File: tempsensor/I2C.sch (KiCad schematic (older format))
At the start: 19 parts, among them J2 Conn_01x04, U2 24C16, U3 MCP9844, U4 SN74LVC2T45DCUR, U5 SN74LVC2T45DCUR

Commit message: Added footprints to tempsensor.
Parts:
- J2: footprint Connector_PinHeader_2.54mm:PinHeader_1x04_P2.54mm_Vertical -> Connector_PinHeader_2.54mm:PinHeader_2x02_P2.54mm_Vertical
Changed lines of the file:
@@
 F 0 "J2" H 3880 7242 50  0000 L CNN
 F 1 "Conn_01x04" H 3880 7151 50  0000 L CNN
-F 2 "Connector_PinHeader_2.54mm:PinHeader_1x04_P2.54mm_Vertical" H 3800 7250 50  0001 C CNN
+F 2 "Connector_PinHeader_2.54mm:PinHeader_2x02_P2.54mm_Vertical" H 3800 7250 50  0001 C CNN
 F 3 "~" H 3800 7250 50  0001 C CNN
 	1    3800 7250

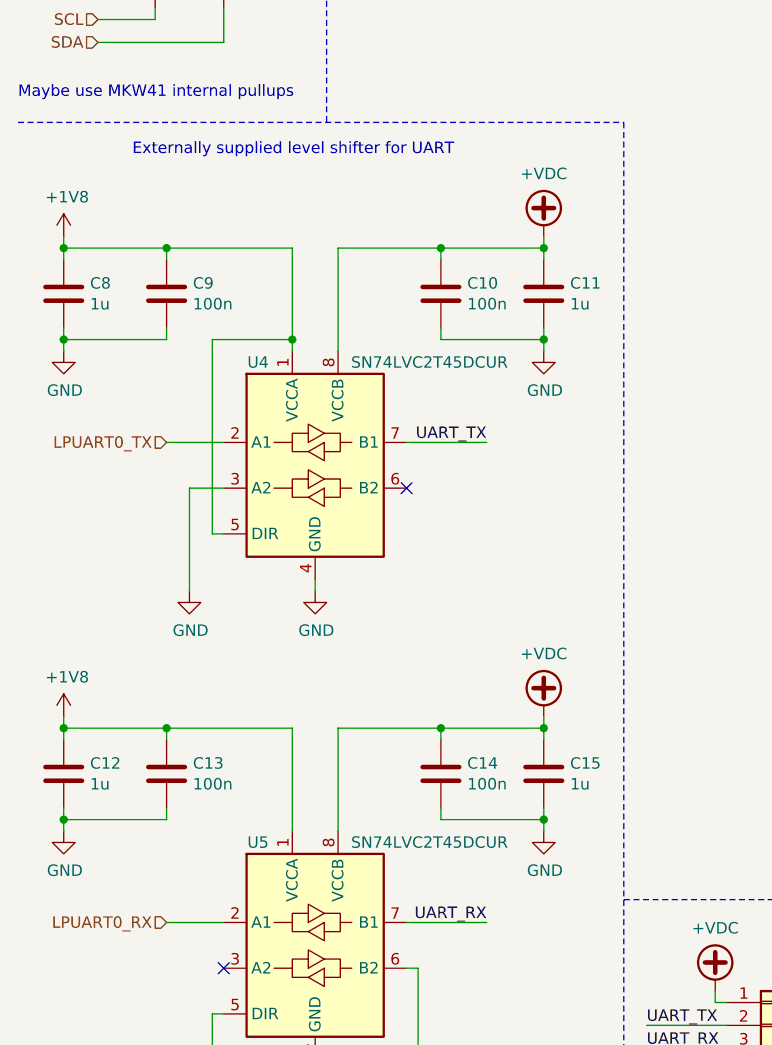
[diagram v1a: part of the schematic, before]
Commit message: Started layouting the TempSensor, exchanged the large LEDs for 0603 LEDs (from ELAB). MCU needs to be placed. Changed signals on expansion header to put power pins onto just one end.
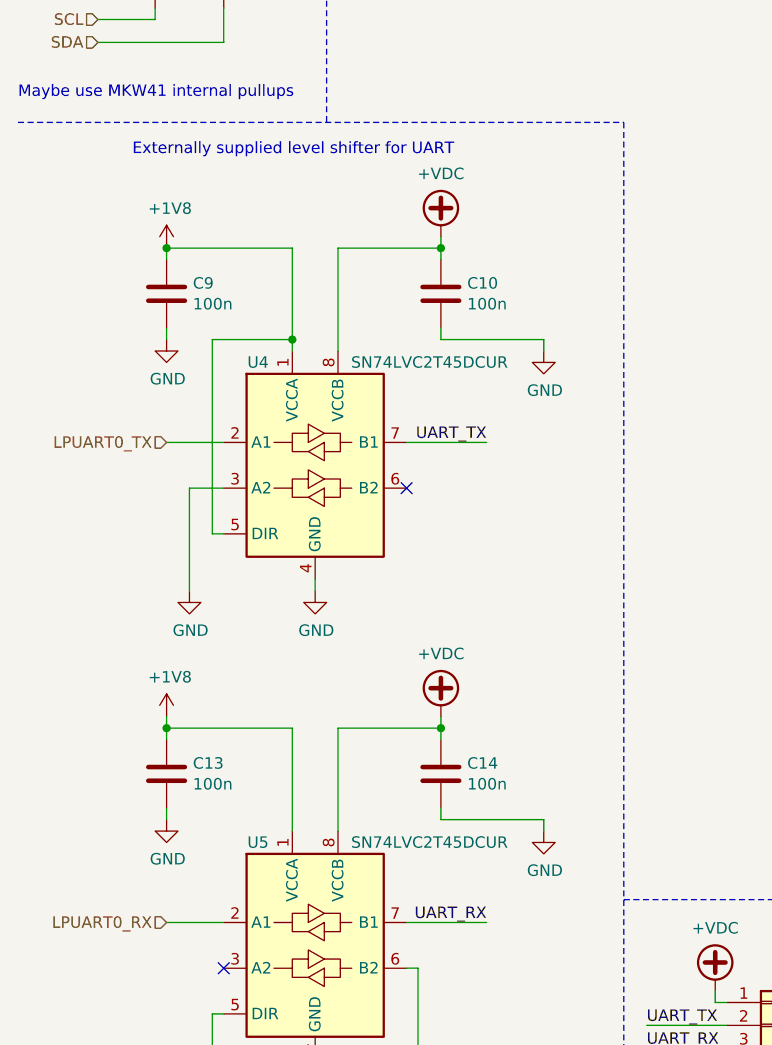
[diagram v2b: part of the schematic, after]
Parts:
- removed C11, C12, C15, C8: 1u, Capacitor_SMD:C_0402_1005Metric, symbol Device:C
- R4: footprint Resistor_SMD:R_0603_1608Metric -> Resistor_SMD:R_0402_1005Metric
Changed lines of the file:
@@
 F 0 "R4" V 5743 3800 50  0000 C CNN
 F 1 "R" V 5834 3800 50  0000 C CNN
-F 2 "Resistor_SMD:R_0603_1608Metric" V 5880 3800 50  0001 C CNN
+F 2 "Resistor_SMD:R_0402_1005Metric" V 5880 3800 50  0001 C CNN
 F 3 "~" H 5950 3800 50  0001 C CNN
 	1    5950 3800
@@
 $Comp
 L Device:C C?
-U 1 1 5FAF3E79
-P 700 4050
-AR Path="/5FAF3E79" Ref="C?"  Part="1"
-AR Path="/5FA4227D/5FAF3E79" Ref="C8"  Part="1"
-F 0 "C8" H 815 4096 50  0000 L CNN
-F 1 "1u" H 815 4005 50  0000 L CNN
-F 2 "Capacitor_SMD:C_0402_1005Metric" H 738 3900 50  0001 C CNN
-F 3 "~" H 700 4050 50  0001 C CNN
-	1    700  4050
-	1    0    0    -1
-$EndComp
-$Comp
-L Device:C C?
 U 1 1 5FAF3E7F
 P 2350 4050
@@
 $EndComp
 $Comp
-L Device:C C?
-U 1 1 5FAF3E85
-P 2800 4050
-AR Path="/5FAF3E85" Ref="C?"  Part="1"
-AR Path="/5FA4227D/5FAF3E85" Ref="C11"  Part="1"
-F 0 "C11" H 2915 4096 50  0000 L CNN
-F 1 "1u" H 2915 4005 50  0000 L CNN
-F 2 "Capacitor_SMD:C_0402_1005Metric" H 2838 3900 50  0001 C CNN
-F 3 "~" H 2800 4050 50  0001 C CNN
-	1    2800 4050
-	1    0    0    -1
-$EndComp
-$Comp
 L power:GND #PWR?
 U 1 1 5FAF3E8B
@@
 	2350 4250 2800 4250
 Wire Wire Line
-	2800 4200 2800 4250
-Wire Wire Line
 	1900 4300 1900 3850
 Wire Wire Line
 	1900 3850 2350 3850
-Wire Wire Line
-	2800 3850 2800 3900
 Wire Wire Line
 	2350 3850 2350 3900
 Connection ~ 2350 3850
 Wire Wire Line
-	2350 3850 2800 3850
-Wire Wire Line
 	1700 4300 1700 4250
 Wire Wire Line
 	1700 3850 1150 3850
 Wire Wire Line
-	700  3850 700  3900
-Wire Wire Line
 	1150 3900 1150 3850
-Connection ~ 1150 3850
-Wire Wire Line
-	1150 3850 700  3850
 Wire Wire Line
 	2800 4300 2800 4250
-Connection ~ 2800 4250
 $Comp
 L power:GND #PWR?
 U 1 1 5FAF3EA2
-P 700 4300
+P 1150 4250
 AR Path="/5FAF3EA2" Ref="#PWR?"  Part="1"
 AR Path="/5FA4227D/5FAF3EA2" Ref="#PWR027"  Part="1"
-F 0 "#PWR027" H 700 4050 50  0001 C CNN
-F 1 "GND" H 705 4127 50  0000 C CNN
-F 2 "" H 700 4300 50  0001 C CNN
-F 3 "" H 700 4300 50  0001 C CNN
-	1    700  4300
-	1    0    0    -1
-$EndComp
-Wire Wire Line
-	700  4200 700  4250
+F 0 "#PWR027" H 1150 4000 50  0001 C CNN
+F 1 "GND" H 1155 4077 50  0000 C CNN
+F 2 "" H 1150 4250 50  0001 C CNN
+F 3 "" H 1150 4250 50  0001 C CNN
+	1    1150 4250
+	1    0    0    -1
+$EndComp
 Wire Wire Line
 	1150 4200 1150 4250
-Wire Wire Line
-	1150 4250 700  4250
-Connection ~ 700  4250
-Wire Wire Line
-	700  4250 700  4300
 $Comp
 L power:+1V8 #PWR?
 U 1 1 5FAF3EAD
-P 700 3800
+P 1150 3850
 AR Path="/5FAF3EAD" Ref="#PWR?"  Part="1"
 AR Path="/5FA4227D/5FAF3EAD" Ref="#PWR025"  Part="1"
-F 0 "#PWR025" H 700 3650 50  0001 C CNN
-F 1 "+1V8" H 715 3973 50  0000 C CNN
-F 2 "" H 700 3800 50  0001 C CNN
-F 3 "" H 700 3800 50  0001 C CNN
-	1    700  3800
-	1    0    0    -1
-$EndComp
-Wire Wire Line
-	700  3800 700  3850
-Connection ~ 700  3850
+F 0 "#PWR025" H 1150 3700 50  0001 C CNN
+F 1 "+1V8" H 1165 4023 50  0000 C CNN
+F 2 "" H 1150 3850 50  0001 C CNN
+F 3 "" H 1150 3850 50  0001 C CNN
+	1    1150 3850
+	1    0    0    -1
+$EndComp
 Text Label 2550 4700 2    50   ~ 0
 UART_TX
@@
 Wire Wire Line
 	1150 4700 1400 4700
-Wire Wire Line
-	2800 3800 2800 3850
-Connection ~ 2800 3850
 $Comp
 L Logic_LevelTranslator:SN74LVC2T45DCUR U?
@@
 $Comp
 L Device:C C?
-U 1 1 5FAF3EDB
-P 700 6150
-AR Path="/5FAF3EDB" Ref="C?"  Part="1"
-AR Path="/5FA4227D/5FAF3EDB" Ref="C12"  Part="1"
-F 0 "C12" H 815 6196 50  0000 L CNN
-F 1 "1u" H 815 6105 50  0000 L CNN
-F 2 "Capacitor_SMD:C_0402_1005Metric" H 738 6000 50  0001 C CNN
-F 3 "~" H 700 6150 50  0001 C CNN
-	1    700  6150
-	1    0    0    -1
-$EndComp
-$Comp
-L Device:C C?
 U 1 1 5FAF3EE1
 P 2350 6150
@@
 $EndComp
 $Comp
-L Device:C C?
-U 1 1 5FAF3EE7
-P 2800 6150
-AR Path="/5FAF3EE7" Ref="C?"  Part="1"
-AR Path="/5FA4227D/5FAF3EE7" Ref="C15"  Part="1"
-F 0 "C15" H 2915 6196 50  0000 L CNN
-F 1 "1u" H 2915 6105 50  0000 L CNN
-F 2 "Capacitor_SMD:C_0402_1005Metric" H 2838 6000 50  0001 C CNN
-F 3 "~" H 2800 6150 50  0001 C CNN
-	1    2800 6150
-	1    0    0    -1
-$EndComp
-$Comp
 L power:GND #PWR?
 U 1 1 5FAF3EED
@@
 	2350 6350 2800 6350
 Wire Wire Line
-	2800 6300 2800 6350
-Wire Wire Line
 	1900 6400 1900 5950
 Wire Wire Line
 	1900 5950 2350 5950
-Wire Wire Line
-	2800 5950 2800 6000
 Wire Wire Line
 	2350 5950 2350 6000
 Connection ~ 2350 5950
 Wire Wire Line
-	2350 5950 2800 5950
-Wire Wire Line
 	1700 5950 1150 5950
 Wire Wire Line
-	700  5950 700  6000
-Wire Wire Line
 	1150 6000 1150 5950
-Connection ~ 1150 5950
-Wire Wire Line
-	1150 5950 700  5950
 Wire Wire Line
 	2800 6400 2800 6350
-Connection ~ 2800 6350
 $Comp
 L power:GND #PWR?
 U 1 1 5FAF3F03
-P 700 6400
+P 1150 6350
 AR Path="/5FAF3F03" Ref="#PWR?"  Part="1"
 AR Path="/5FA4227D/5FAF3F03" Ref="#PWR035"  Part="1"
-F 0 "#PWR035" H 700 6150 50  0001 C CNN
-F 1 "GND" H 705 6227 50  0000 C CNN
-F 2 "" H 700 6400 50  0001 C CNN
-F 3 "" H 700 6400 50  0001 C CNN
-	1    700  6400
-	1    0    0    -1
-$EndComp
-Wire Wire Line
-	700  6300 700  6350
+F 0 "#PWR035" H 1150 6100 50  0001 C CNN
+F 1 "GND" H 1155 6177 50  0000 C CNN
+F 2 "" H 1150 6350 50  0001 C CNN
+F 3 "" H 1150 6350 50  0001 C CNN
+	1    1150 6350
+	1    0    0    -1
+$EndComp
 Wire Wire Line
 	1150 6300 1150 6350
-Wire Wire Line
-	1150 6350 700  6350
-Connection ~ 700  6350
-Wire Wire Line
-	700  6350 700  6400
 $Comp
 L power:+1V8 #PWR?
 U 1 1 5FAF3F0E
-P 700 5900
+P 1150 5900
 AR Path="/5FAF3F0E" Ref="#PWR?"  Part="1"
 AR Path="/5FA4227D/5FAF3F0E" Ref="#PWR033"  Part="1"
-F 0 "#PWR033" H 700 5750 50  0001 C CNN
-F 1 "+1V8" H 715 6073 50  0000 C CNN
-F 2 "" H 700 5900 50  0001 C CNN
-F 3 "" H 700 5900 50  0001 C CNN
-	1    700  5900
-	1    0    0    -1
-$EndComp
-Wire Wire Line
-	700  5900 700  5950
-Connection ~ 700  5950
+F 0 "#PWR033" H 1150 5750 50  0001 C CNN
+F 1 "+1V8" H 1165 6073 50  0000 C CNN
+F 2 "" H 1150 5900 50  0001 C CNN
+F 3 "" H 1150 5900 50  0001 C CNN
+	1    1150 5900
+	1    0    0    -1
+$EndComp
 Wire Wire Line
 	1400 7200 1350 7200
@@
 	1150 6800 1400 6800
 Wire Wire Line
-	2800 5900 2800 5950
-Connection ~ 2800 5950
-Wire Wire Line
 	2550 4700 2200 4700
 Wire Wire Line
@@
 L power:+VDC #PWR?
 U 1 1 5FAF3F36
-P 2800 3800
+P 2350 3800
 AR Path="/5FAF3F36" Ref="#PWR?"  Part="1"
 AR Path="/5FA4227D/5FAF3F36" Ref="#PWR026"  Part="1"
-F 0 "#PWR026" H 2800 3700 50  0001 C CNN
-F 1 "+VDC" H 2800 4075 50  0000 C CNN
-F 2 "" H 2800 3800 50  0001 C CNN
-F 3 "" H 2800 3800 50  0001 C CNN
-	1    2800 3800
+F 0 "#PWR026" H 2350 3700 50  0001 C CNN
+F 1 "+VDC" H 2350 4075 50  0000 C CNN
+F 2 "" H 2350 3800 50  0001 C CNN
+F 3 "" H 2350 3800 50  0001 C CNN
+	1    2350 3800
 	1    0    0    -1
 $EndComp
@@
 L power:+VDC #PWR?
 U 1 1 5FAF3F3C
-P 2800 5900
+P 2350 5900
 AR Path="/5FAF3F3C" Ref="#PWR?"  Part="1"
 AR Path="/5FA4227D/5FAF3F3C" Ref="#PWR034"  Part="1"
-F 0 "#PWR034" H 2800 5800 50  0001 C CNN
-F 1 "+VDC" H 2800 6175 50  0000 C CNN
-F 2 "" H 2800 5900 50  0001 C CNN
-F 3 "" H 2800 5900 50  0001 C CNN
-	1    2800 5900
+F 0 "#PWR034" H 2350 5800 50  0001 C CNN
+F 1 "+VDC" H 2350 6175 50  0000 C CNN
+F 2 "" H 2350 5900 50  0001 C CNN
+F 3 "" H 2350 5900 50  0001 C CNN
+	1    2350 5900
 	1    0    0    -1
 $EndComp
@@
 Wire Wire Line
 	5700 4000 5950 4000
+Wire Wire Line
+	2350 3800 2350 3850
+Connection ~ 1150 3850
+Wire Wire Line
+	2350 5900 2350 5950
+Wire Wire Line
+	1150 5900 1150 5950
+Connection ~ 1150 5950
 $EndSCHEMATC

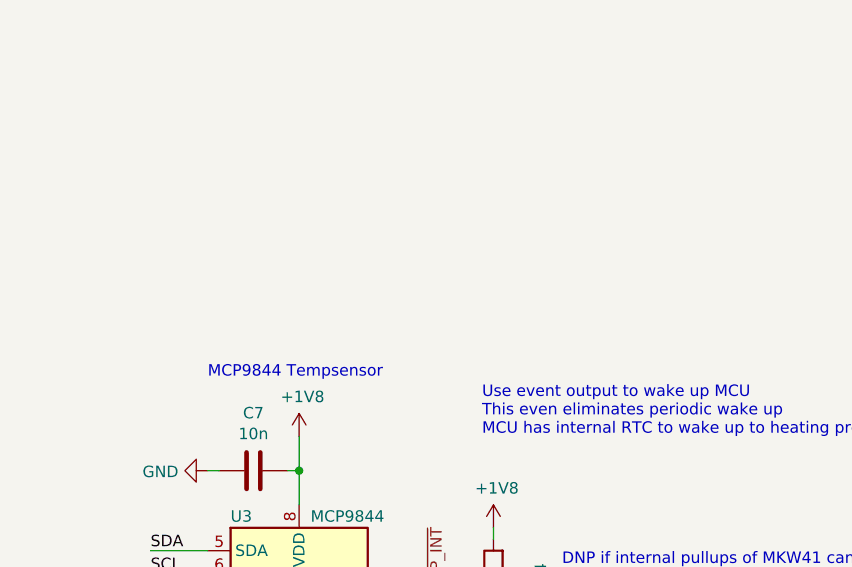
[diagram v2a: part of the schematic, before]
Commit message: Continued routing of tempsensor, basic functionality done.
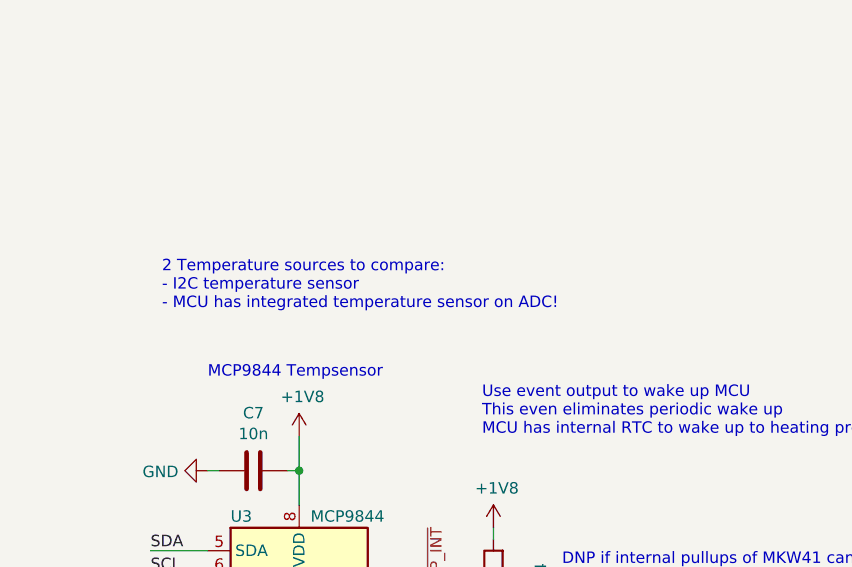
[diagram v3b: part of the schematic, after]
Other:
- note added: "2 Temperature sources to compare:\n- I2C temperature sensor\n- MCU has integrated temperature sensor on ADC!"
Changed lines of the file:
@@
 	1150 5900 1150 5950
 Connection ~ 1150 5950
+Text Notes 4500 2650 0    50   ~ 0
+2 Temperature sources to compare:\n- I2C temperature sensor\n- MCU has integrated temperature sensor on ADC!
 $EndSCHEMATC
